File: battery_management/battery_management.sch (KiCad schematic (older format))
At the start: 9 parts, among them J1 Conn_02x20_Odd_Even, U1 L7805

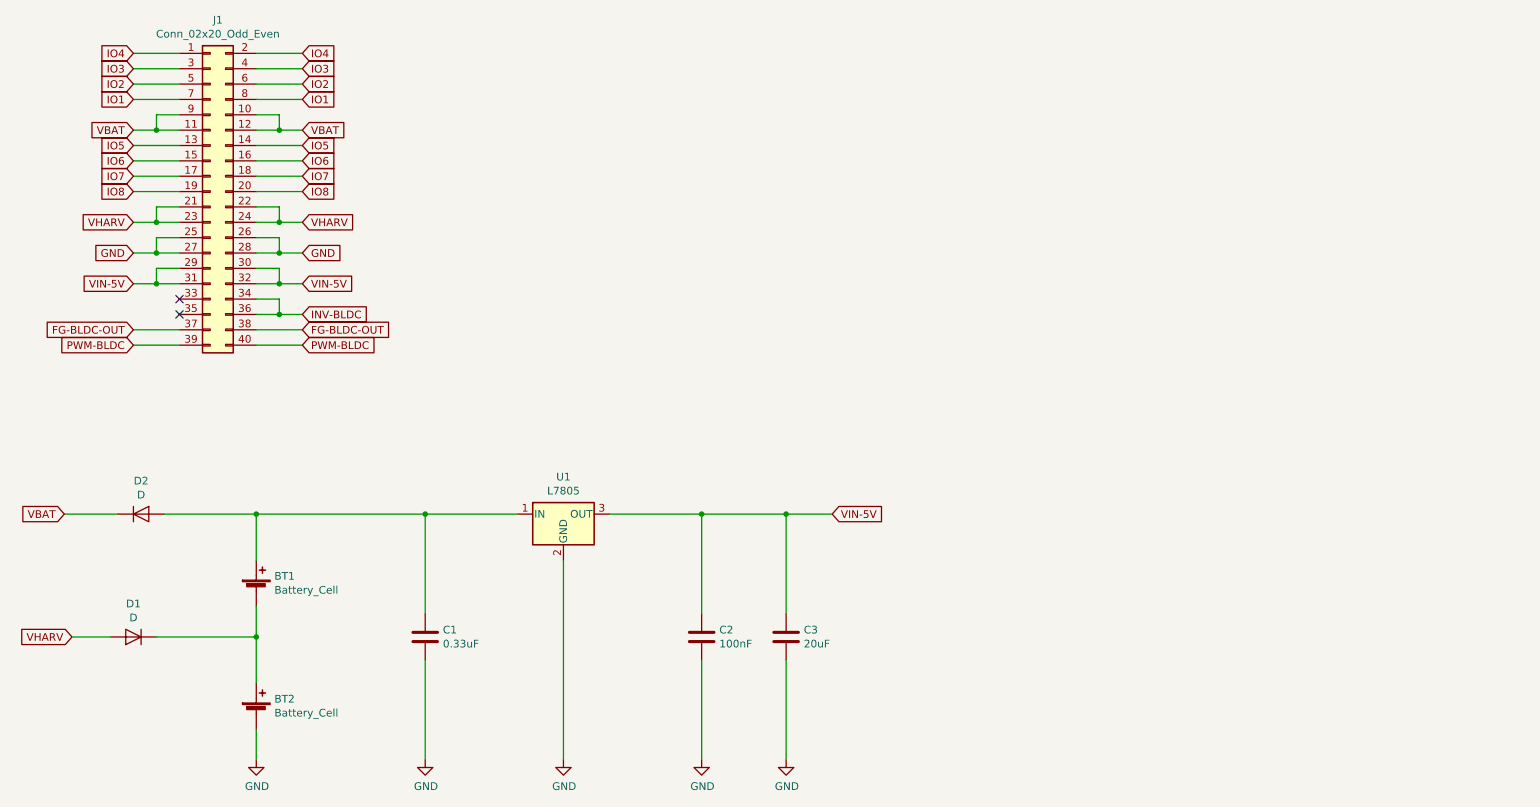
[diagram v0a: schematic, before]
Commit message: esquemático semi-pronto v0.2
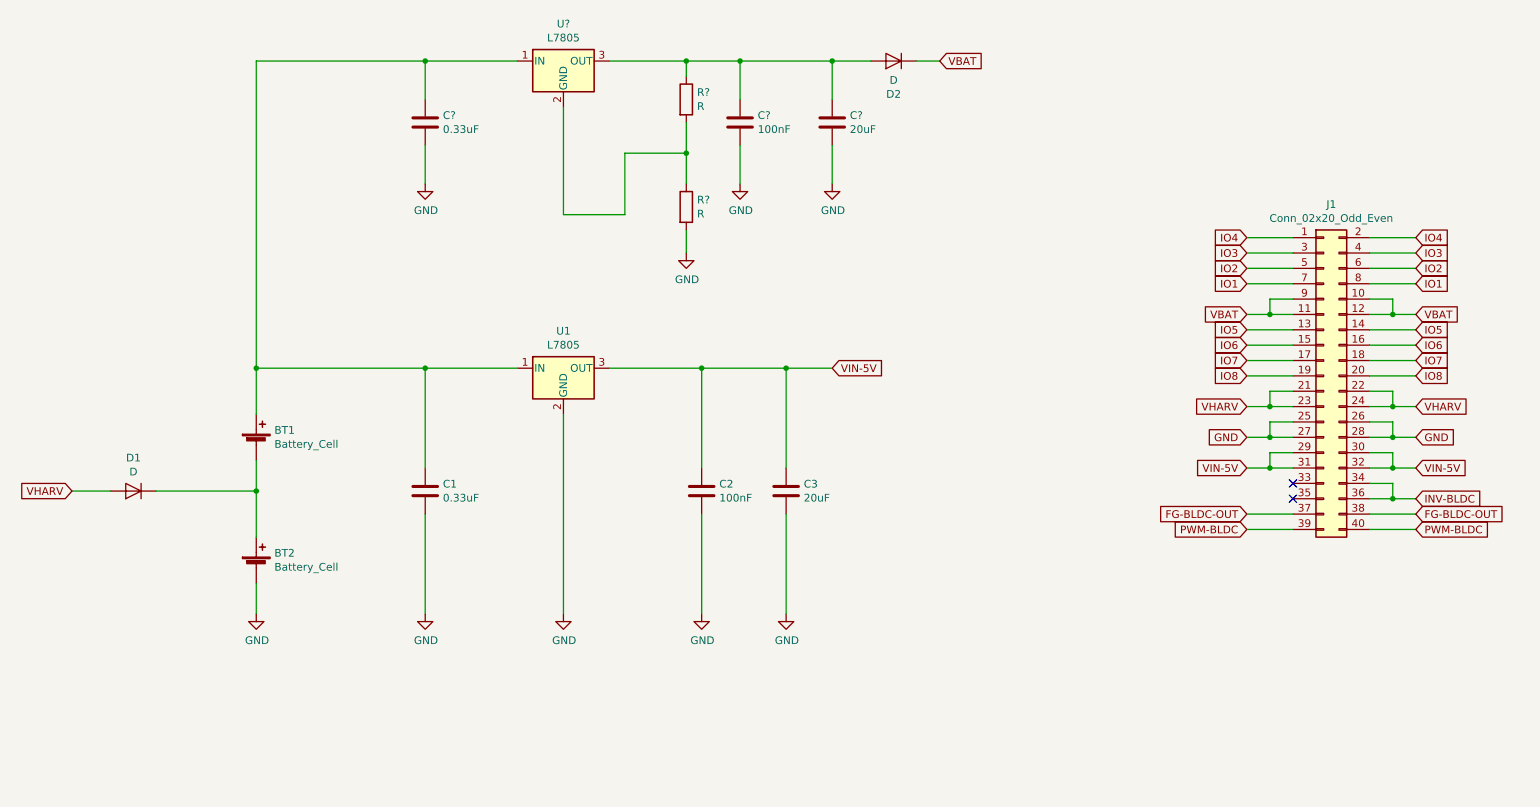
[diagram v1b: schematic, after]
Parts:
- added C?: 0.33uF, Capacitor_THT:C_Rect_L7.0mm_W6.0mm_P5.00mm, symbol Device:C
- added C?: 100nF, Capacitor_THT:C_Rect_L7.0mm_W6.0mm_P5.00mm, symbol Device:C
- added C?: 20uF, Capacitor_THT:C_Rect_L7.0mm_W6.0mm_P5.00mm, symbol Device:C
- added R? (x2): R, symbol Device:R
- added U?: L7805, Package_TO_SOT_THT:TO-220-3_Horizontal_TabDown, symbol Regulator_Linear:L7805
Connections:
- net GND: now also C?.2, C?.2, C?.2, R?.2
- net at BT1.1 (+), C1.1, U1.1 (IN): now also C?.1, U?.1 (IN); no longer D2.2 (A)
- new net: C?.1, C?.1, D2.2 (A), R?.1, U?.3 (OUT)
- new net: R?.1, R?.2, U?.2 (GND)
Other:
- moved on the sheet: BT1, BT2, C1, C2, C3, D1, D2, J1, U1
